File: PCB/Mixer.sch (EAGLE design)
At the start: 132 parts, among them U1 TL074IDT, U10 POWER, U11 TL074IDT, U12 3PDTSWITCH, U2 TL074IDT, U3 TL074IDT, U4 TL074IDT, U5 TL074IDT, U6 TL074IDT, U7 TL074IDT, U8 22PINHEADER22PINHEADER, U9 22PINHEADER22PINHEADER

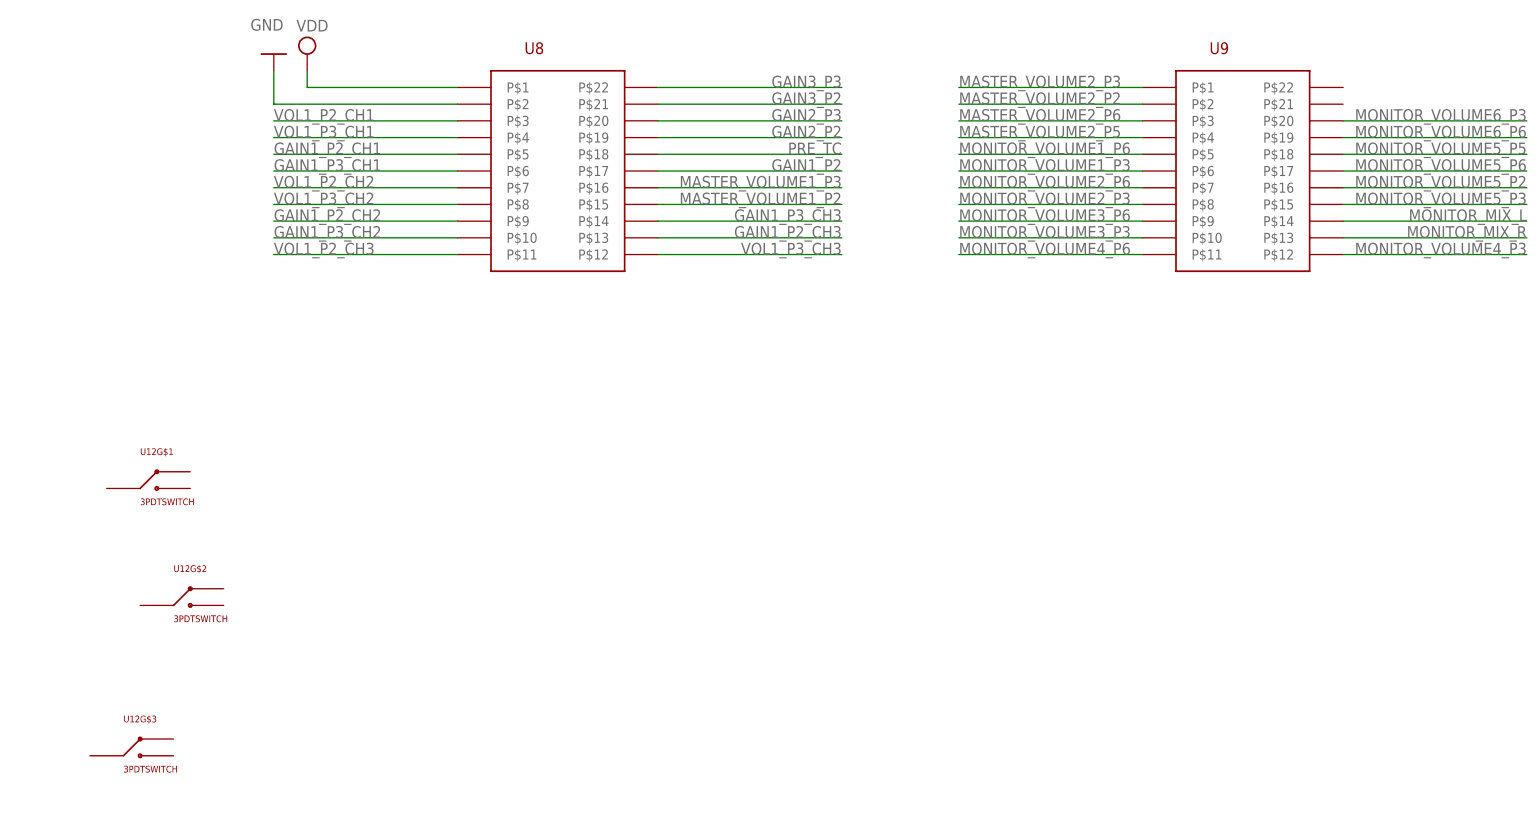
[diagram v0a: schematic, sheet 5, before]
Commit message: Add switch and analog selectors
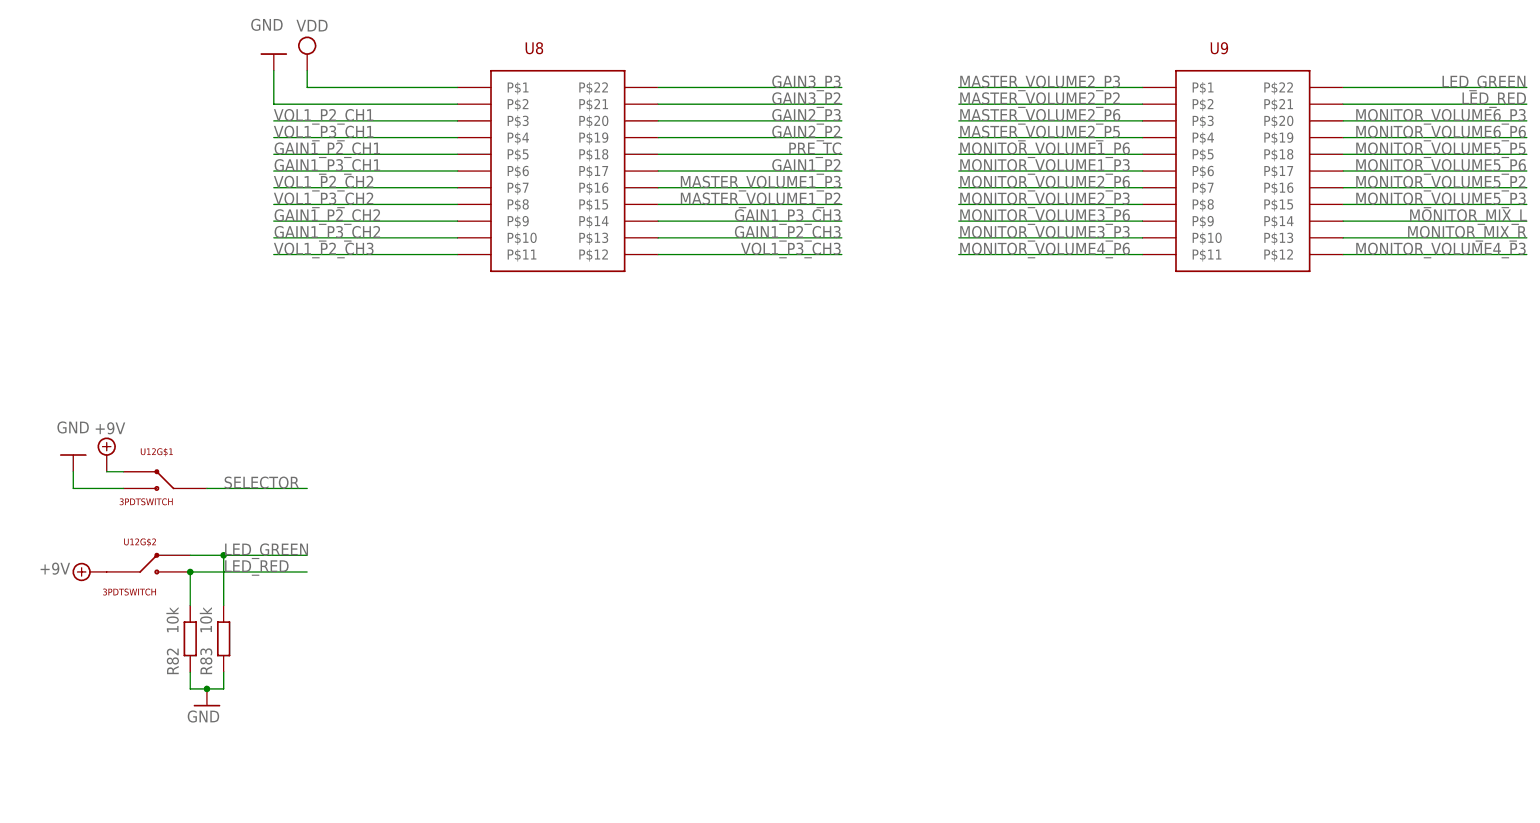
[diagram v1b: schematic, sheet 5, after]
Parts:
- added R82, R83: 10k, lib:RESISTOR
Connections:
- new net LED_GREEN: R83.2, U12G$2.1, U9.P$22
- new net LED_RED: R82.2, U12G$2.3, U9.P$21
- new net SELECTOR: U12G$1.2
- net +9V: now also U12G$1.1, U12G$2.2
- net GND: now also R82.1, R83.1, U12G$1.3
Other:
- moved on the sheet: U12G$1, U12G$2

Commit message: Semi done
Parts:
- added C31, C32: 100n/16V, lib:CAPACITORC-0603
- added C33: 10u / 16V, lib:CAPACITORC-0603
- added R84: 1k, lib:RESISTOR
- added U13: ISL43240IAZ, lib:ANALOG_SELECTORSSOP-20
- added U14: ISL43410IUZ, lib:2CH_ANALOG_SELECTORMSOP-10
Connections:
- removed net MONITOR_VOLUME5_P4: U7G$4.IN+
- new net MASTER_BYP: R20.1, U14.NC1, U14.NC2, U2G$1.IN-, U2G$1.OUT
- new net MASTER_OUT_L: U14.COM2, U5G$4.IN+, U6G$1.IN+
- new net MASTER_OUT_R: U14.COM1, U3G$1.IN+, U5G$2.IN+
- new net SR-BYPASS: R10.2, R5.2, R8.1, U2G$1.OUT
- new net SR-OUT: R17.2
- new net SR-SELECT: R16.1
- new net SR_BYP_CH1: U13.NC1
- new net SR_BYP_CH2: U13.NC2
- new net SR_BYP_CH3: U13.NC3
- new net SR_OUT_CH1: U13.NO1
- new net SR_OUT_CH2: U13.NO2
- new net SR_OUT_CH3: U13.NO3
- new net SR_SEL_CH1: U13.COM1
- new net SR_SEL_CH2: U13.COM2
- new net SR_SEL_CH3: U13.COM3
- net +9V: now also C30.2, C31.1, C32.1, C33.2, U13.V+, U14.V+, U6G$5.V+
- net GAIN1_P3: now also R17.1; no longer R16.1
- net GND: now also C30.1, C31.2, C32.2, C33.1, U12G$3.1, U12G$3.2, U12G$3.3, U13.GND, U13.V-, U14.GND, U14.INH, U6G$5.V-
- net MASTER_RETURN_L: now also U14.NO2; no longer U5G$4.IN+, U6G$1.IN+
- net MASTER_RETURN_R: now also U14.NO1; no longer U3G$1.IN+, U5G$2.IN+
- net MONITOR_VOLUME5_P5: now also U7G$4.IN+
- net N$13: no longer R10.2, R5.2, R8.1, U2G$1.OUT
- net N$15: now also R84.1, U12G$1.2; no longer R20.1, U2G$1.IN-, U2G$1.OUT
- net SELECTOR: now also R84.2, U13.IN1, U13.IN2, U13.IN3, U13.IN4, U14.ADD; no longer U12G$1.2
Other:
- moved on the sheet: C1, C11, C12, C17, C27, C4, C5, R1, R17, R18, R2, R41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

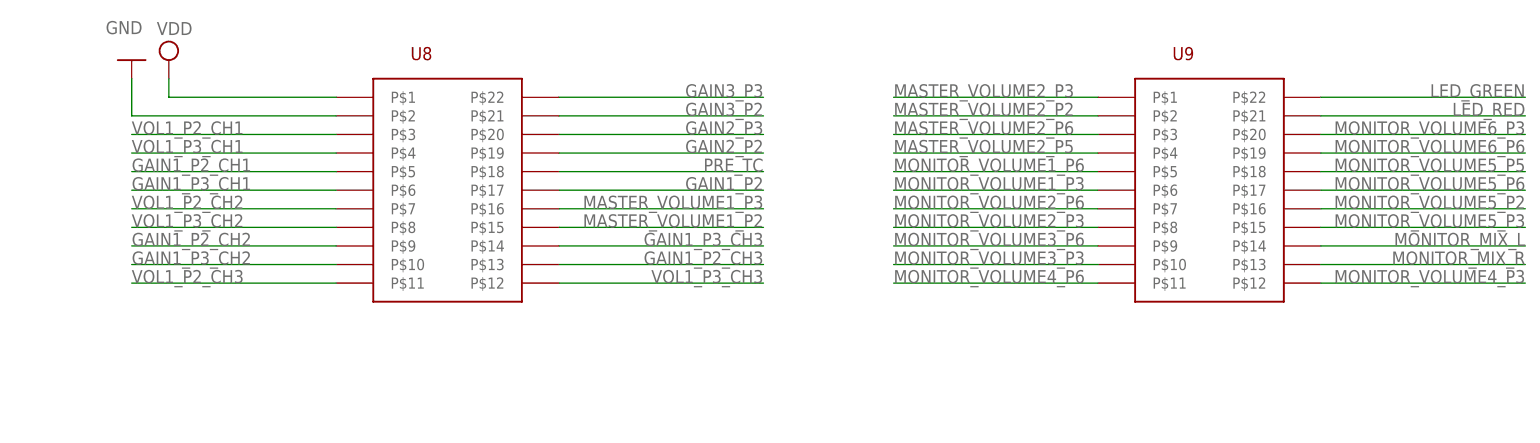
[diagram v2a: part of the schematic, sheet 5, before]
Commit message: Updating to 2 layer
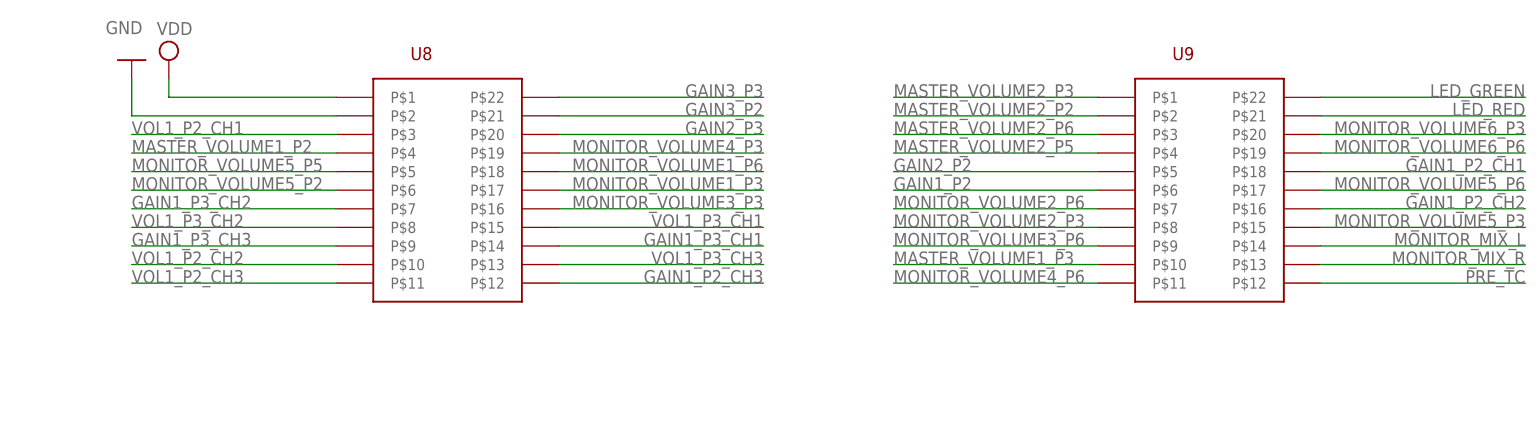
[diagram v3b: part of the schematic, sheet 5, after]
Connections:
- new net OUT: U2G$3.IN-, U2G$3.OUT
- net CH1_OUT: now also U1G$2.IN+; no longer U1G$1.IN+
- net CH2_OUT: now also U1G$1.IN+; no longer U1G$2.IN+
- net CH3_OUT: now also U1G$4.IN+; no longer U1G$3.IN+
- net GAIN1_P2: now also U9.P$6; no longer U8.P$17
- net GAIN1_P2_CH1: now also U9.P$18; no longer U8.P$5
- net GAIN1_P2_CH2: now also U9.P$16; no longer U8.P$9
- net GAIN1_P2_CH3: now also U8.P$12; no longer U8.P$13
- net GAIN1_P3_CH1: now also U8.P$14; no longer U8.P$6
- net GAIN1_P3_CH2: now also U8.P$7; no longer U8.P$10
- net GAIN1_P3_CH3: now also U8.P$9; no longer U8.P$14
- net GAIN2_P2: now also U9.P$5; no longer U8.P$19
- net MASTER_VOLUME1_P2: now also U8.P$4; no longer U8.P$15
- net MASTER_VOLUME1_P3: now also U1G$3.OUT, U9.P$10; no longer U1G$4.OUT, U8.P$16
- net MONITOR_VOLUME1_P3: now also U8.P$17; no longer U9.P$6
- net MONITOR_VOLUME1_P6: now also U8.P$18; no longer U9.P$5
- net MONITOR_VOLUME3_P3: now also U8.P$16; no longer U9.P$10
- net MONITOR_VOLUME4_P3: now also U8.P$19; no longer U9.P$12
- net MONITOR_VOLUME5_P2: now also U8.P$6; no longer U9.P$16
- net MONITOR_VOLUME5_P5: now also U8.P$5; no longer U9.P$18
- net N$1: now also U1G$3.IN+; no longer U1G$4.IN+
- net N$2: now also U1G$3.IN-; no longer U1G$4.IN-
- net N$33: now also U1G$2.IN-, U1G$2.OUT; no longer U1G$1.IN-, U1G$1.OUT
- net N$36: now also U1G$1.IN-, U1G$1.OUT; no longer U1G$2.IN-, U1G$2.OUT
- net N$39: now also U1G$4.IN-, U1G$4.OUT; no longer U1G$3.IN-, U1G$3.OUT
- net N$9: no longer U2G$3.IN-, U2G$3.OUT
- net PRE_TC: now also U9.P$12; no longer U8.P$18
- net SR_BYP_CH1: now also U13.NC2; no longer U13.NC1
- net SR_BYP_CH2: now also U13.NC1; no longer U13.NC2
- net SR_OUT_CH1: now also U13.NO2; no longer U13.NO1
- net SR_OUT_CH2: now also U13.NO1; no longer U13.NO2
- net SR_SEL_CH1: now also U13.COM2; no longer U13.COM1
- net SR_SEL_CH2: now also U13.COM1; no longer U13.COM2
- net VOL1_P2_CH2: now also U8.P$10; no longer U8.P$7
- net VOL1_P3_CH1: now also U8.P$15; no longer U8.P$4
- net VOL1_P3_CH3: now also U8.P$13; no longer U8.P$12
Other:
- moved on the sheet: U1G$1, U1G$2, U1G$3, U1G$4
